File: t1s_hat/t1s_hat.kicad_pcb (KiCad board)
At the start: 2 copper layers, 66.2 x 49.2 mm, 41 parts, among them CN1 T1S BUS P N N P, J1 2x20 socket (riser stack), U1 LAN8651, Y1 25.000MHz

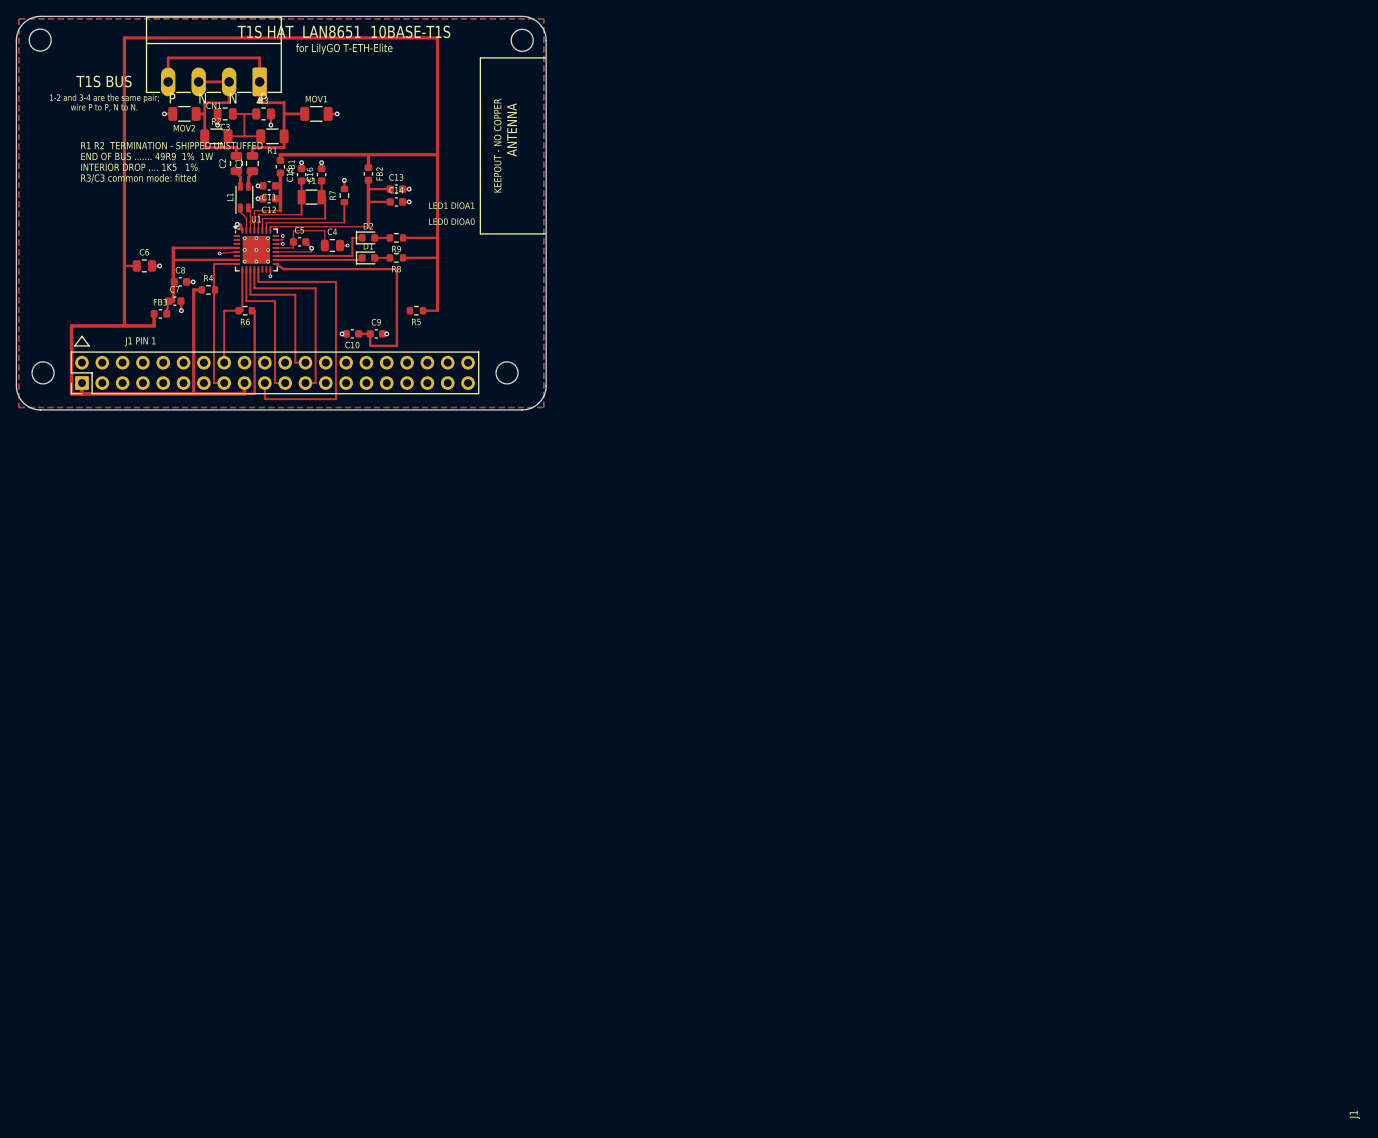
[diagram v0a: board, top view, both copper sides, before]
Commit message: T1S HAT: real choke and varistor lands, both nets closed, silk cleaned
The choke was the fabrication blocker. L1 sat on KiCad's 1206 4-terminal
land (3.2 x 1.6 mm) while every part AN1718 names is 3.2 x 2.5 mm, so the
real component's terminals missed the pads. AN1718 says its part numbers
are examples and the customer picks, so pick one that can be bought:
TDK ACT1210L-201-2P-TL00, 200 uH @ 100 kHz (inside the 130..240 uH span
the three examples cover), AEC-Q200, LCSC C131444. Its land is drawn from
TDK's own ACT1210 layout recommendation -- 4.1 x 1.6 mm overall, 2.0 and
0.4 mm gaps -- into a new project footprint library, and the symbol moves
to L_Coupled_1423 because the ACT1210's windings are 1-4 and 2-3.

MOV1/MOV2 got the same treatment. ELECTRICAL.md already names
TDK AVRH10C221KT1R5YA8, which is a 1005 [0402] part; the board had it on
a 1206 resistor land. Now on a 0402 land taken from TDK's AVR catalogue
recommended pattern. LCSC C2157827. Still DNP.

Both unrouted nets are closed, unrouted count 0, with nothing on B.Cu:

  SPI_CS_N  R5 moved to straddle the MISO column -- MISO passes between
            its own pads. No extra part.
  VDDP      JP1, a real 0 ohm 0603, straddling the +3V3 branch on the
            left edge. In the schematic (net split VDDP / VDDP_17, each
            with its own PWR_FLAG), in the BOM as "fit", and on the silk.

Silkscreen: 48 violations to 0. Designators are now placed by the
generator, which tries each one in a ring around its own part and keeps
the first position clear of every pad, via, ink and the board edge; none
had to be dropped. Board text re-laid into the pad-free areas, CN1's
per-pad letters replaced by a legend, pin-1 marker is a dot.

The all-layer void under the choke is sized to the part: maximum body
3.9 x 2.7 mm plus 0.25 mm a side. It grew in x only because the part did.

Verified: mechanical worst error 0.00000 mm, antenna keepout 0 intruders,
B.Cu signal tracks 0, unrouted 0, ERC 0 errors / 5 warnings, D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
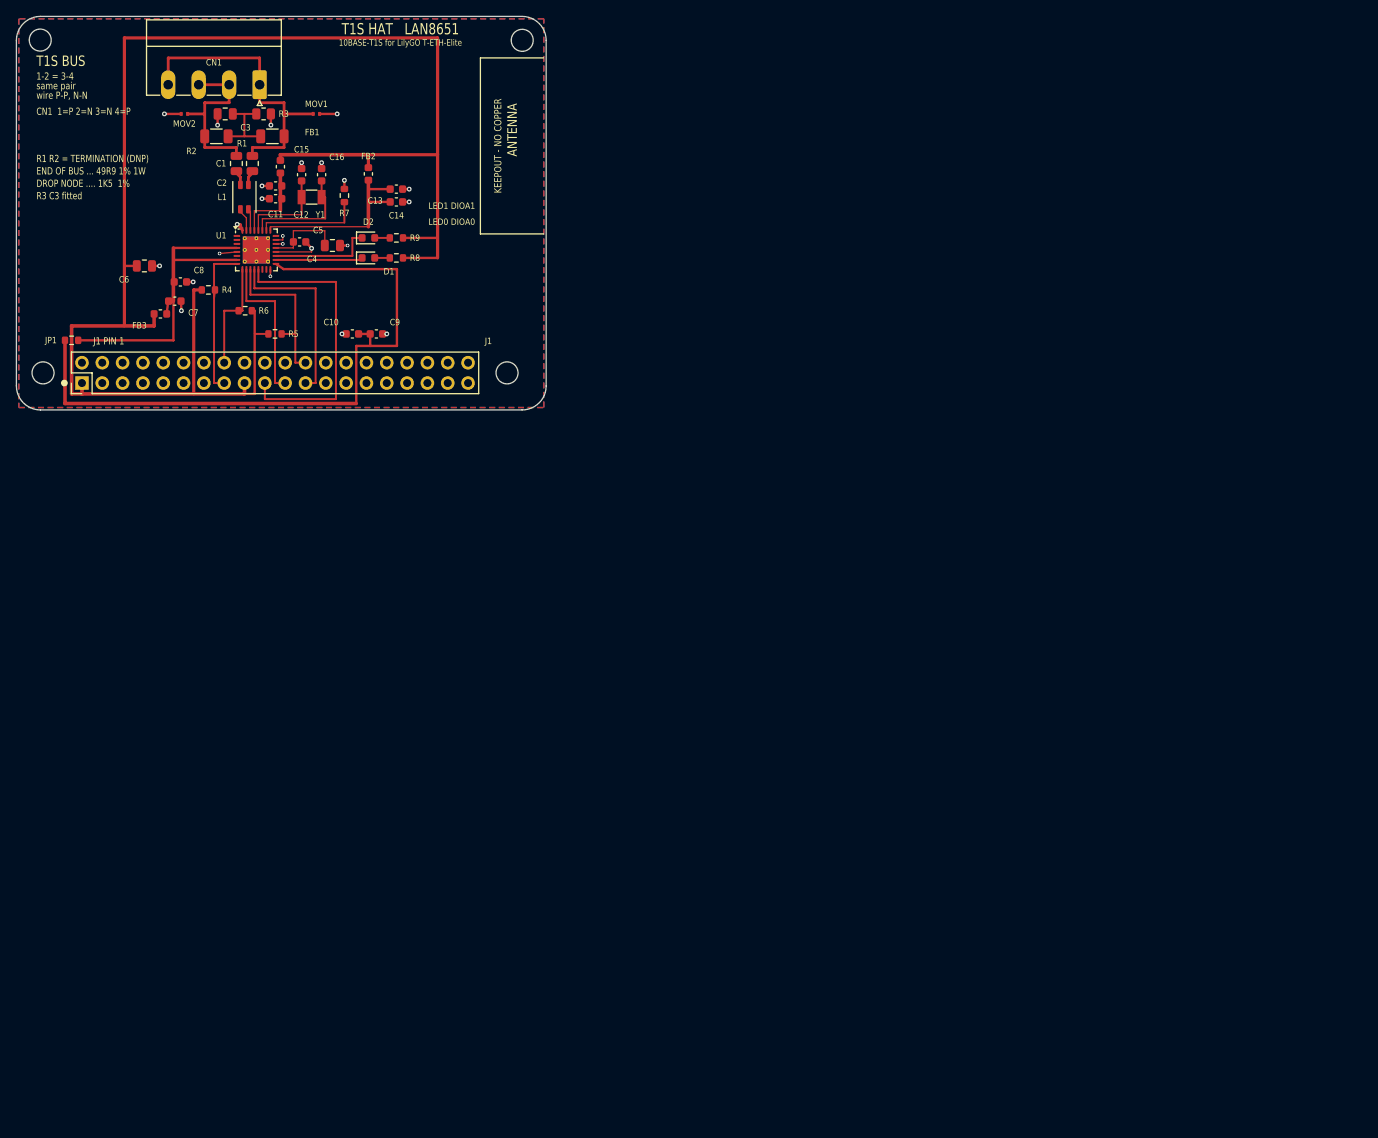
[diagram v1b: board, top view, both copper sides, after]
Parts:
- added JP1: 0R jumper, Resistor_SMD:R_0603_1608Metric, F.Cu at (106.9, 91.3)
- L1: value 130uH @ 100kHz CMC -> 200uH @ 100kHz CMC; footprint Inductor_SMD:L_CommonMode_Wurth_WE-CNSW-1206 -> t1s_hat:L_CommonMode_TDK_ACT1210_3225
- MOV1, MOV2: value ESD 1206 (DNP) -> 22V 1.5pF ESD (DNP); footprint Resistor_SMD:R_1206_3216Metric -> t1s_hat:Varistor_TDK_AVRH10_1005
- moved R5 17.9 mm to (132.3, 90.5), turned to 0 degrees
- moved C11 0.80 mm to (132.4, 72.0)
- moved C12 0.80 mm to (132.4, 73.6)
- moved CN1 0.35 mm to (130.4, 59.4)
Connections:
- C10 pad 1: VDDP -> VDDP_17
- C9 pad 1: VDDP -> VDDP_17
- L1 pad 1: TRXN -> TRXP
- L1 pad 2: CMC_N -> TRXN
- L1 pad 3: CMC_P -> CMC_N
- L1 pad 4: TRXP -> CMC_P
- U1 pad 17: VDDP -> VDDP_17
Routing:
- net VDDP_17: track 0.00 -> 84.5 mm
- net VDDP: track 61.9 -> 47.4 mm
- net +3V3: track 213.9 -> 207.2 mm
- net GND: track 28.8 -> 31.6 mm
- net SPI_CS_N: track 18.5 -> 20.3 mm
- net BUS_P: track 36.3 -> 37.7 mm
- net VDDA: track 11.7 -> 10.8 mm
- net BUS_N: track 21.2 -> 21.9 mm
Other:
- board text added: "1-2 = 3-4"
- board text added: "10BASE-T1S for LilyGO T-ETH-Elite"
- board text added: "CN1 1=P 2=N 3=N 4=P"
- board text added: "DROP NODE .... 1K5 1%"
- board text added: "END OF BUS ... 49R9 1% 1W"
- board text added: "R1 R2 = TERMINATION (DNP)"
- board text added: "R3 C3 fitted"
- board text added: "T1S HAT LAN8651"
- board text added: "same pair"
- board text added: "wire P-P, N-N"
- board text removed: "1-2 and 3-4 are the same pair;"
- board text removed: "END OF BUS ....... 49R9 1% 1W"
- board text removed: "INTERIOR DROP .... 1K5 1%"
- board text removed: "N"
- board text removed: "P"
- board text removed: "R1 R2 TERMINATION - SHIPPED UNSTUFFED"
- board text removed: "R3/C3 common mode: fitted"
- board text removed: "T1S HAT LAN8651 10BASE-T1S"
- board text removed: "for LilyGO T-ETH-Elite"
- board text removed: "wire P to P, N to N."
